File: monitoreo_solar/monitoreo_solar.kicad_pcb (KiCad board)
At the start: 2 copper layers, 50 x 45 mm, 25 parts, among them J1 Screw_Terminal_01x02, J2 Conn_01x03_Socket, J3 Screw_Terminal_01x02, J4 Conn_01x04_Pin, J5 Conn_01x03_Pin, U1 X9C103S, U2 AMS1117-3.3, U4 LM358

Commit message: first pcb design
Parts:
- H1, H2, H3, H4: footprint MountingHole:MountingHole_5mm -> MountingHole:MountingHole_3.2mm_M3
- U1: moved to B.Cu
- moved J2 97.6 mm to (27.2, 66.5)
- moved J4 94.7 mm to (41.0, 60.4), turned to -90 degrees
- moved U4 83.6 mm to (41.9, 75.2)
- moved C2 70.5 mm to (35.2, 66.0), turned to 180 degrees
- moved R1 68.7 mm to (24.9, 76.5)
- moved C5 68.3 mm to (38.2, 92.5), turned to 180 degrees
- moved C1 65.2 mm to (40.6, 64.9), turned to -90 degrees
- moved D2 61.1 mm to (61.5, 59.2), turned to 180 degrees
- moved J5 60.9 mm to (68.4, 69.1)
- moved D1 55.1 mm to (61.5, 65.1), turned to 180 degrees
- moved R2 54.7 mm to (38.0, 74.4), turned to -90 degrees
- moved C4 54.0 mm to (55.9, 96.2), turned to 180 degrees
- moved U2 50.7 mm to (42.8, 96.4)
- moved R4 50.6 mm to (41.3, 71.2), turned to 180 degrees
- moved J3 47.9 mm to (67.3, 89.0), turned to 90 degrees
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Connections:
- J4 pad 1: GND -> +3.3V
- J4 pad 4: +3.3V -> GND
- J5 pad 2: DIR -> STEP
- J5 pad 3: STEP -> DIR
- R3 pad 1: Vout -> Pot+
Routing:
- net +5V: track 0.00 -> 136.0 mm
- net GND: track 0.00 -> 106.1 mm
- net +3.3V: track 0.00 -> 77.8 mm
- net Net-(D2-A): track 0.00 -> 24.3 mm
- net Pot-: track 0.00 -> 21.0 mm
- net Net-(D1-A): track 0.00 -> 18.5 mm
- net Pot+: track 0.00 -> 16.8 mm
- net Net-(U4B-+): track 0.00 -> 14.7 mm
- net POT_CS: track 0.00 -> 13.1 mm
- net Net-(U4A-+): track 0.00 -> 11.6 mm
- net Vpanel: track 0.00 -> 8.60 mm
- net Vcurrent: track 0.00 -> 8.42 mm
- net Vamp1: track 0.00 -> 6.80 mm
- net STEP: track 0.00 -> 6.14 mm
- net DIR: track 0.00 -> 5.62 mm

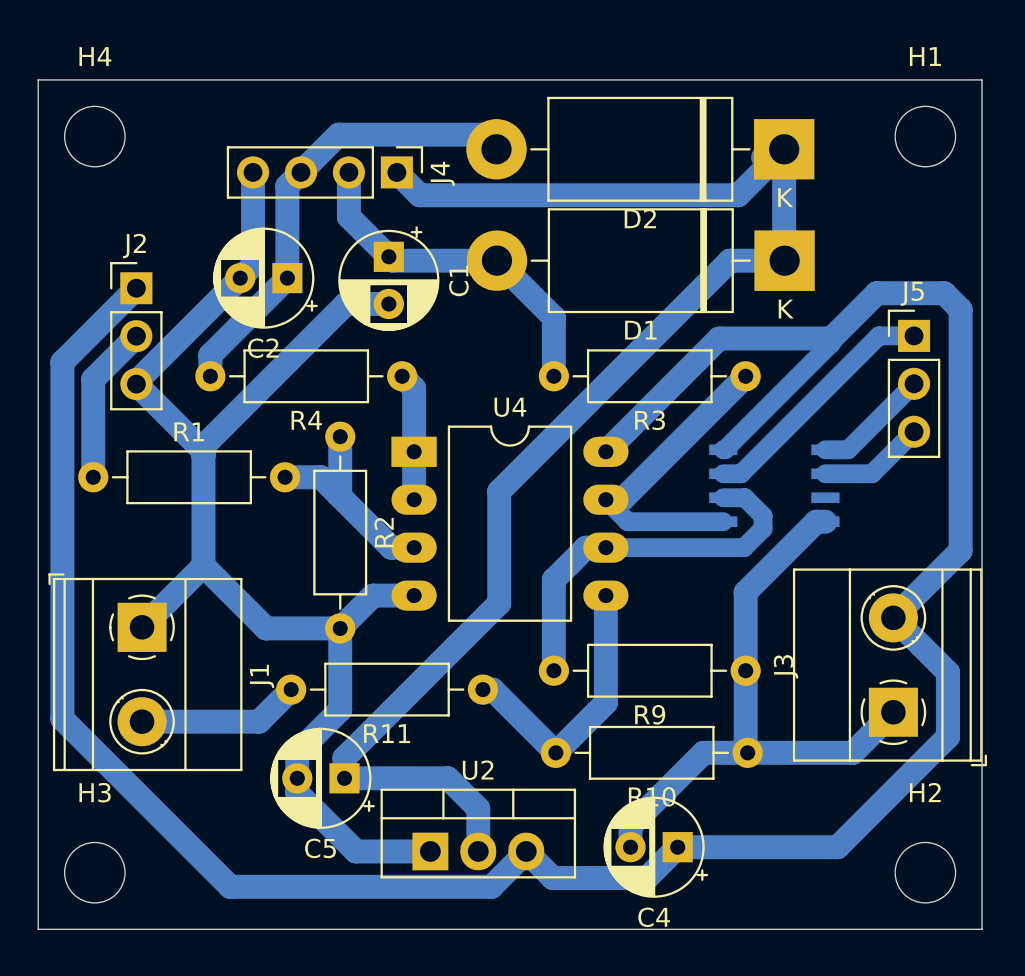
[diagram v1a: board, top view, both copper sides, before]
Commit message: feat: v2 pcb con board potenciometro a medida
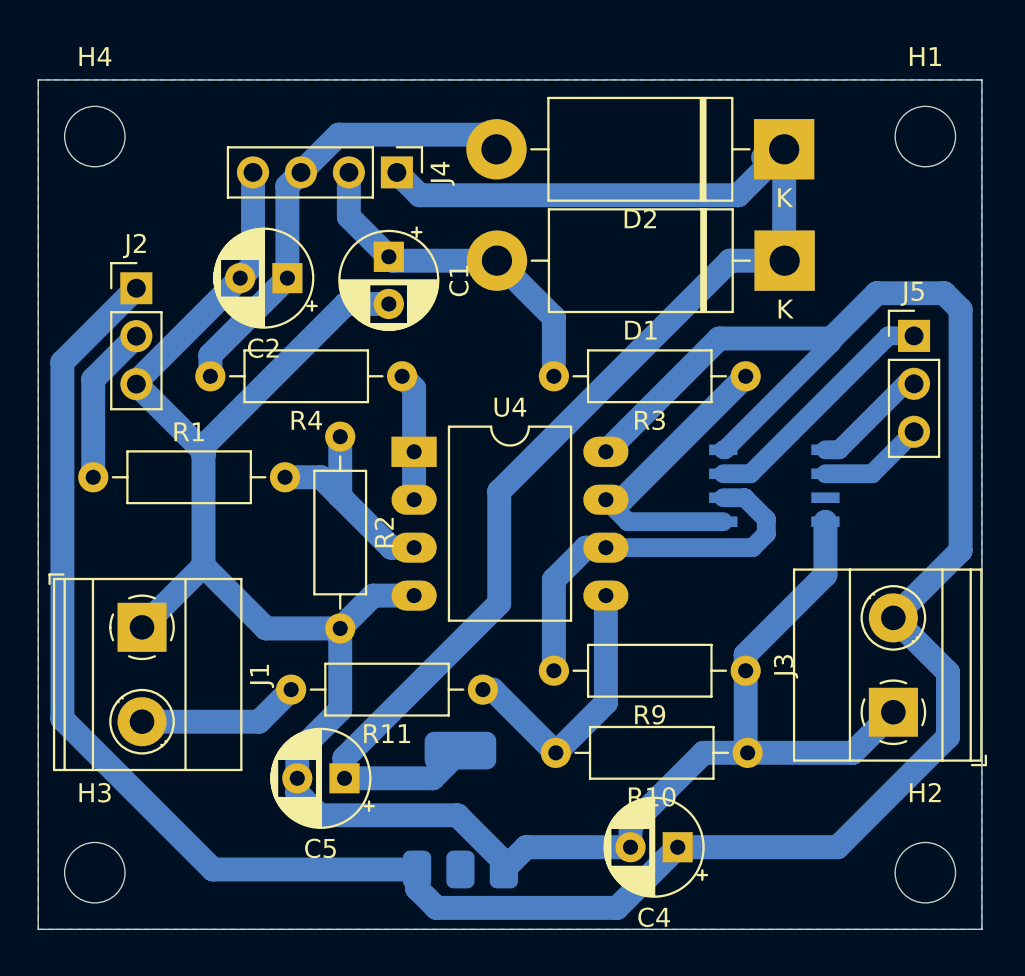
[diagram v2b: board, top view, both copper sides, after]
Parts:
- U2: footprint Package_TO_SOT_THT:TO-220-3_Vertical -> Package_TO_SOT_SMD:SOT-223-3_TabPin2; moved to B.Cu
- moved U2 2.71 mm to (44.4, 94.2), turned to 90 degrees
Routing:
- net GND: track 106.1 -> 117.5 mm
- net +3.3V: track 77.8 -> 74.5 mm
- added copper zone on B.Cu, net GND
